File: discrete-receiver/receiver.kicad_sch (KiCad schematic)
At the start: 27 parts, among them J1 His Excellence, J3 Conn_01x04_Socket, J7 Her Excellency, T1 H1102NLT, T2 MABA-007159-000000, U5 ADE-12+

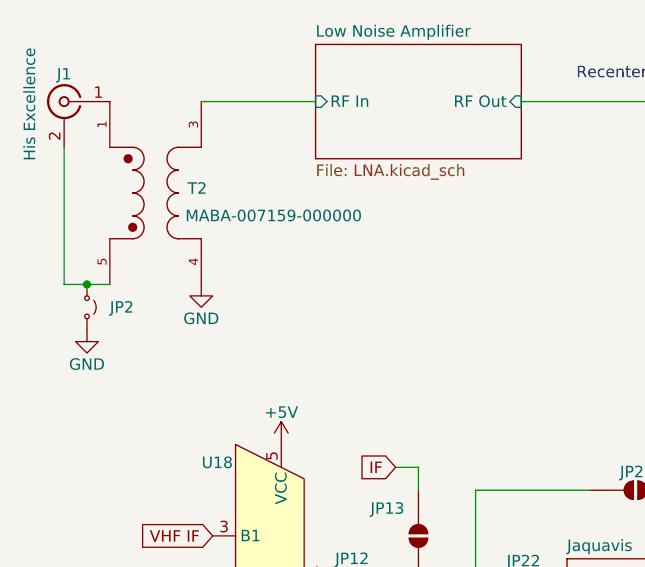
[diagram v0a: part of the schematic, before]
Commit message: Redone draft of power page
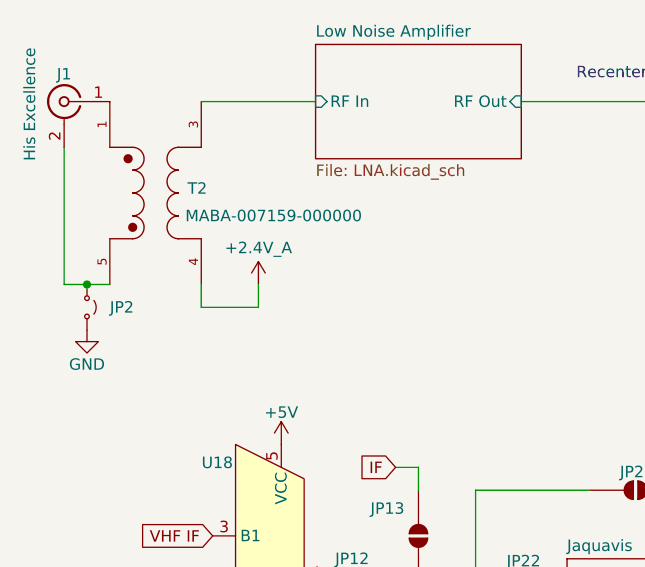
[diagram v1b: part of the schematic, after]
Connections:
- net GND: no longer T2.4
- new net +2.4V_A: T2.4

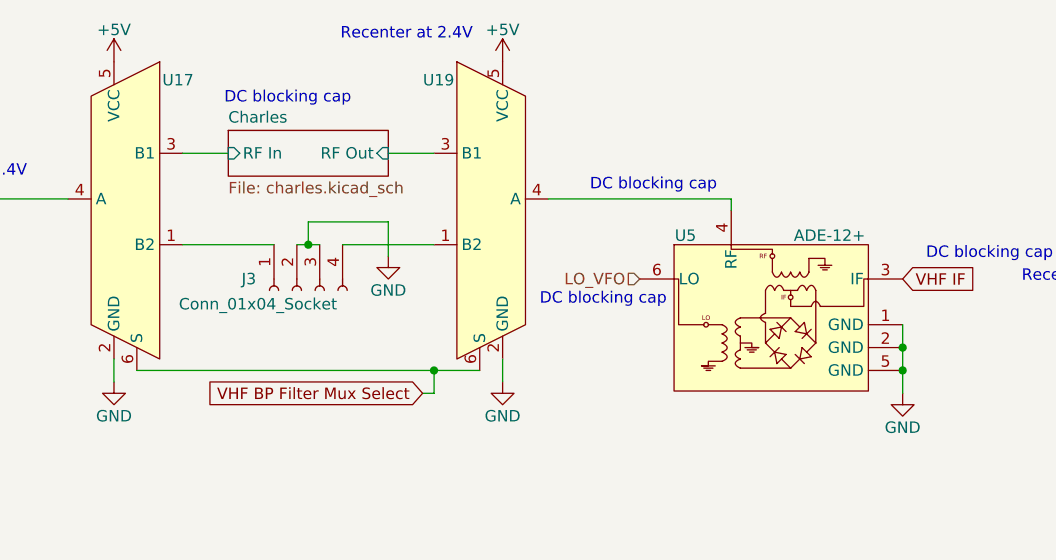
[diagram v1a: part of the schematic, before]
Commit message: Switched from ADE-12+ to ADE-1+
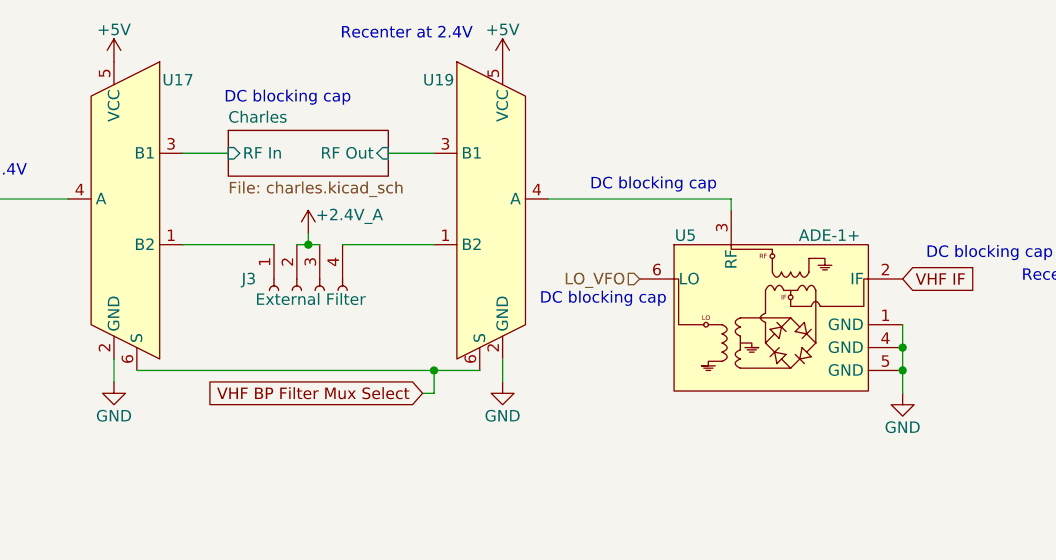
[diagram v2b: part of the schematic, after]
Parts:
- J3: value Conn_01x04_Socket -> External Filter
- U5: value ADE-12+ -> ADE-1+; LCSC C3176671 -> C2942210
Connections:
- net +2.4V_A: now also J3.2 (Pin_2), J3.3 (Pin_3)
- net GND: now also U5.4 (GND); no longer J3.2 (Pin_2), J3.3 (Pin_3), U5.2 (GND)
- net VHF IF: now also U5.2 (IF); no longer U5.3 (IF)
- net at U19.4 (A): now also U5.3 (RF); no longer U5.4 (RF)

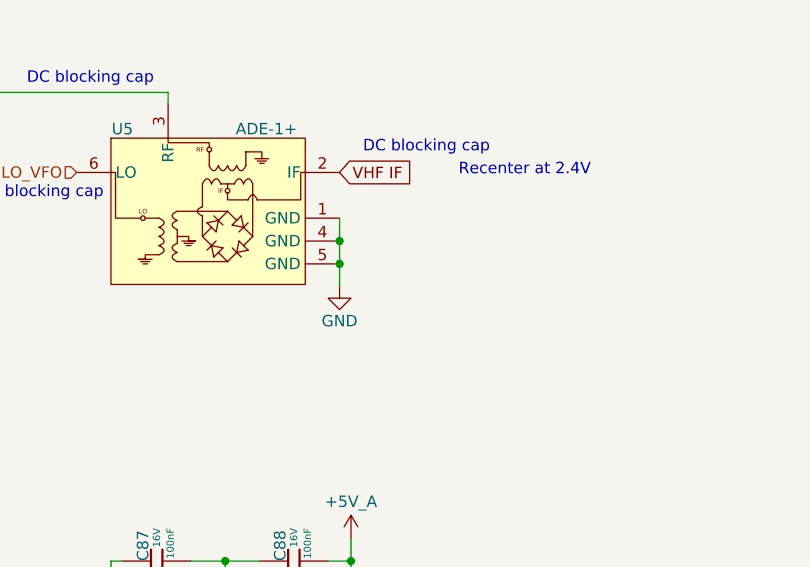
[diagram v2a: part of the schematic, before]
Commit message: Improved POE power filtering and added test points
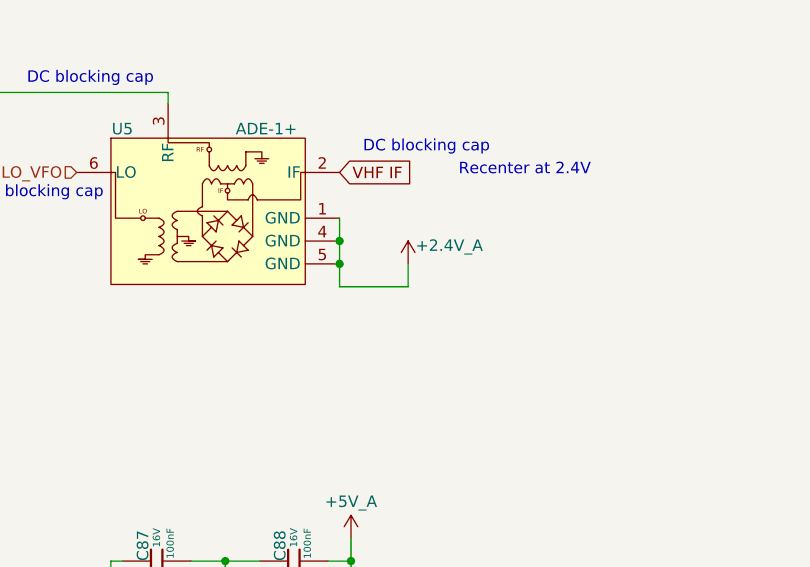
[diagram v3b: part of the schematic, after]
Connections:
- net +2.4V_A: now also U5.1 (GND), U5.4 (GND), U5.5 (GND)
- net GND: no longer U5.1 (GND), U5.4 (GND), U5.5 (GND)

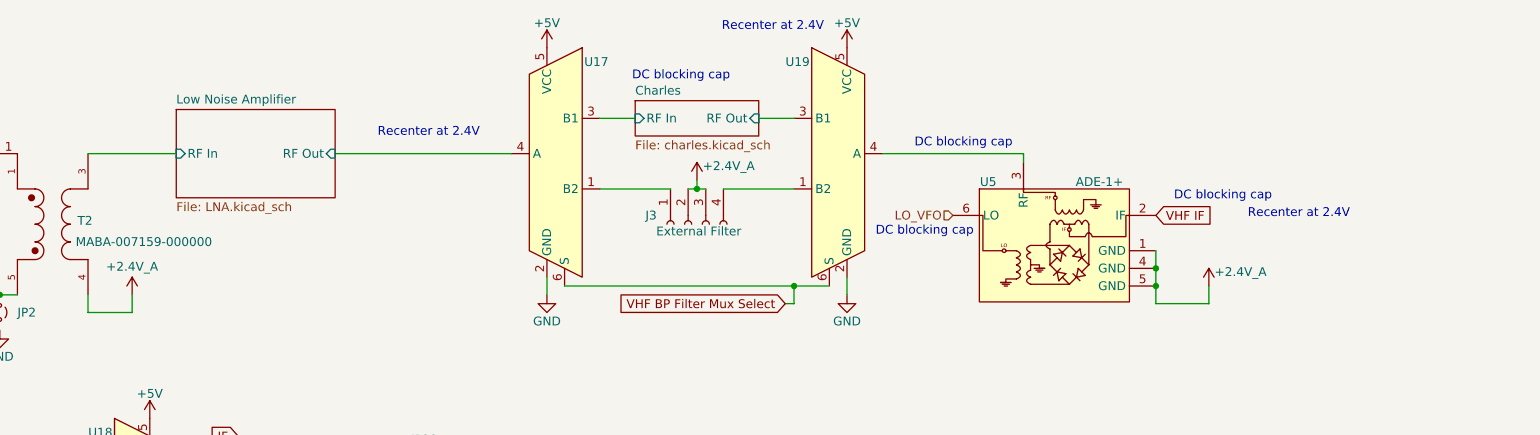
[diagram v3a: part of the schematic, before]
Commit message: Added DC blocking capacitor to diode ring mixer LO input.
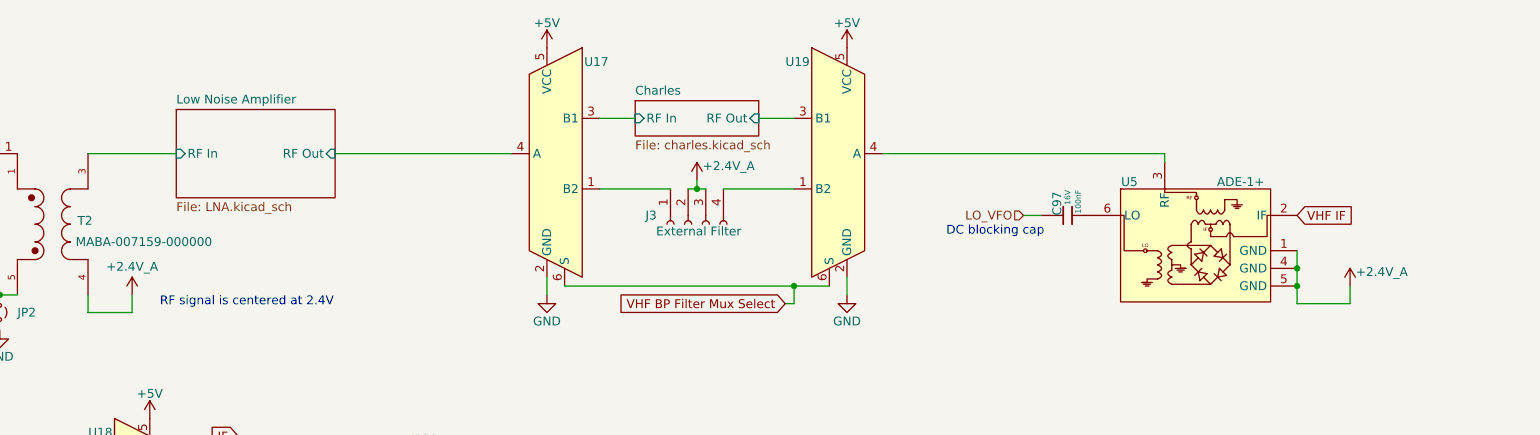
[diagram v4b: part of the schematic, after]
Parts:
- added C97: 100nF, PCM_JLCPCB:C_0402, symbol PCM_JLCPCB-Capacitors:0402,100nF
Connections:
- net LO_VFO: now also C97.1; no longer U5.6 (LO)
- new net: C97.2, U5.6 (LO)
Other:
- note added: "RF signal is centered at 2.4V"
- note removed: "Recenter at 2.4V"
- moved on the sheet: U5

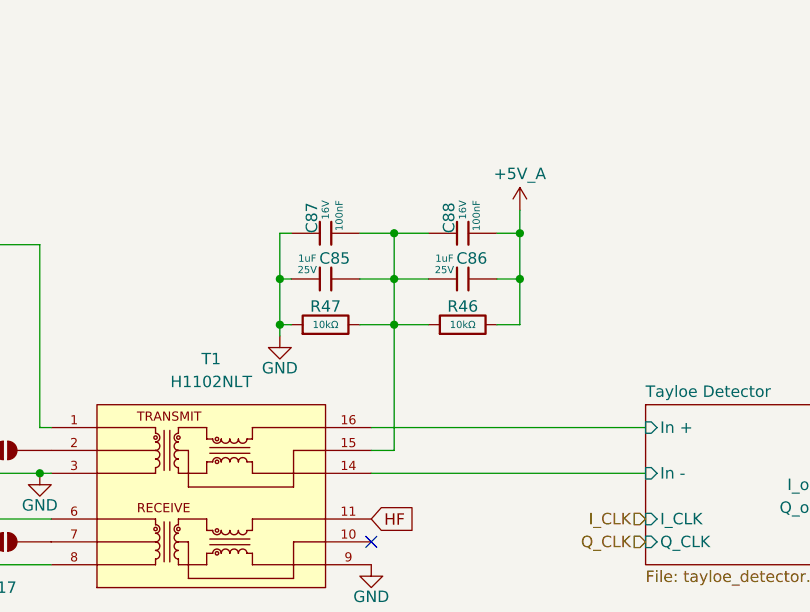
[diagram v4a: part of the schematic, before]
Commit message: Fixed RF grounds
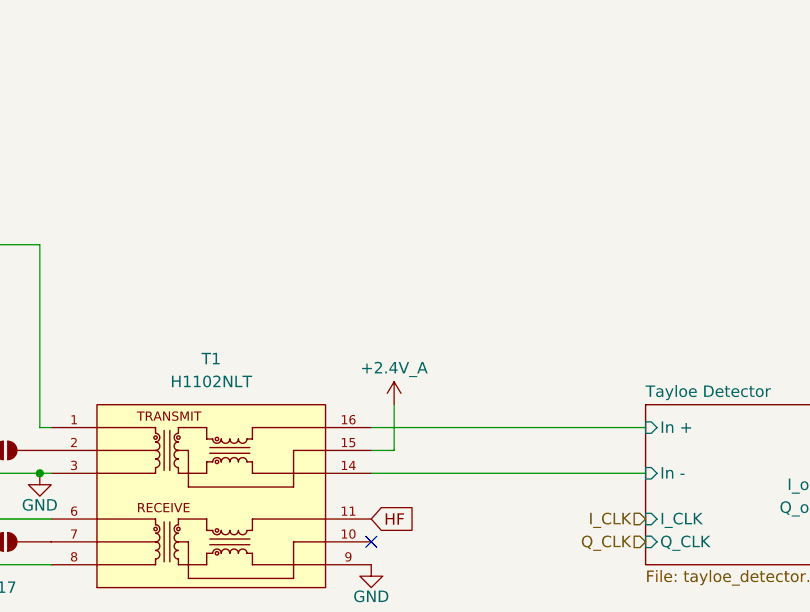
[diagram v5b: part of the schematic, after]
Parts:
- removed C85, C86: 1uF, PCM_JLCPCB:C_0402, symbol PCM_JLCPCB-Capacitors:0402,1uF
- removed C87, C88: 100nF, PCM_JLCPCB:C_0402, symbol PCM_JLCPCB-Capacitors:0402,100nF
- removed R46, R47: 10kΩ, PCM_JLCPCB:R_0402, symbol PCM_JLCPCB-Resistors:0402,10kΩ
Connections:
- net +2.4V_A: now also T1.15

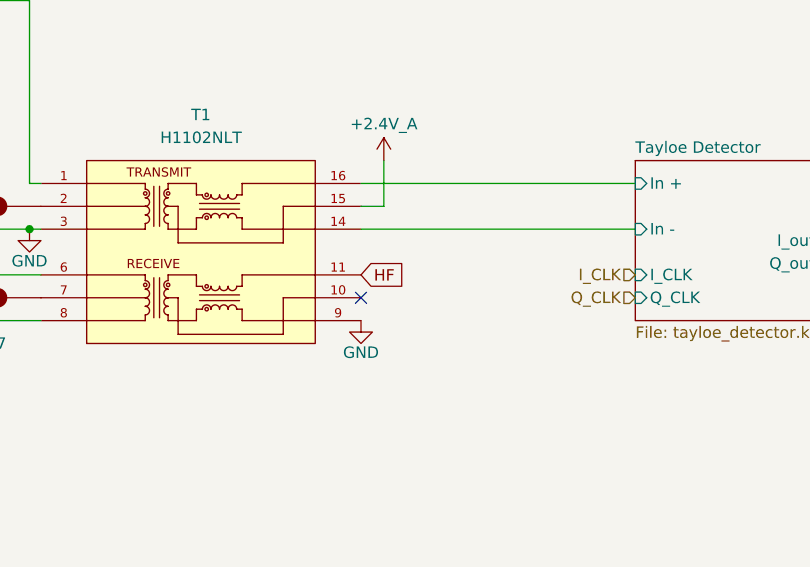
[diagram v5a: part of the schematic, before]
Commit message: Fixed RF ground for HF transformer
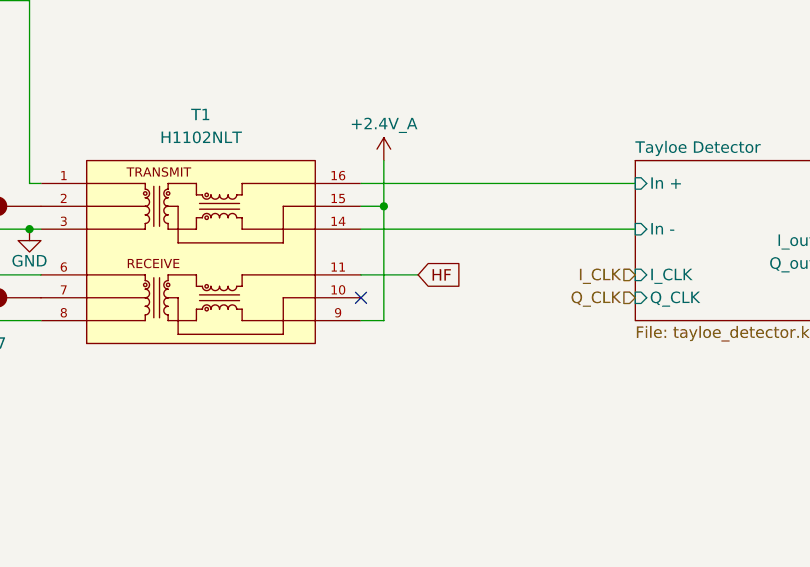
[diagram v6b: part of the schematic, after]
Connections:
- net +2.4V_A: now also T1.9
- net GND: no longer T1.9
